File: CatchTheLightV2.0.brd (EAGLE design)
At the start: 45 x 100 mm, 42 parts, among them J1 TC2030-IDC-NL, U1 ATMEGA328PB-MUR

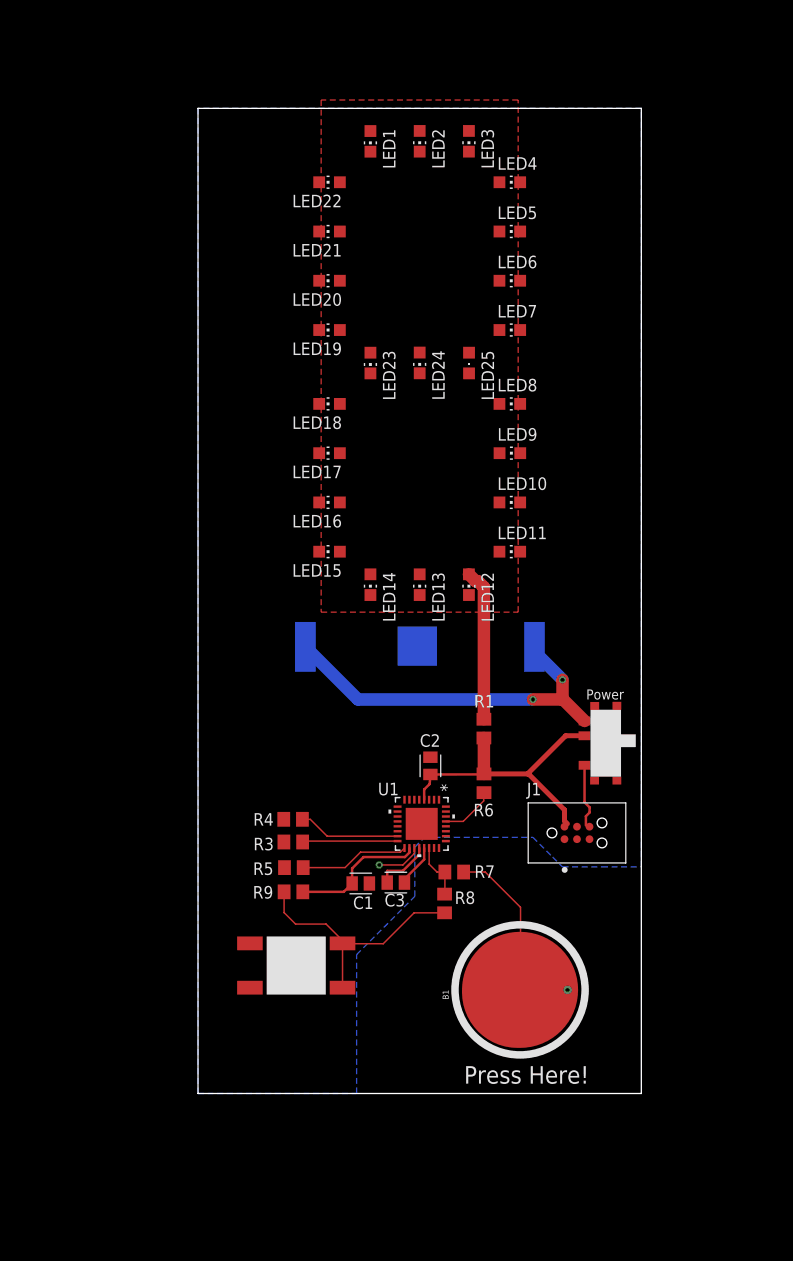
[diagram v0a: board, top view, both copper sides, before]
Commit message: Revised Schematic and Board design to use correct 328pb footprint
Modified a whole lot. New approach to board design. Will try to fill in all wiring first, and then draw in the rest of the pours/planes
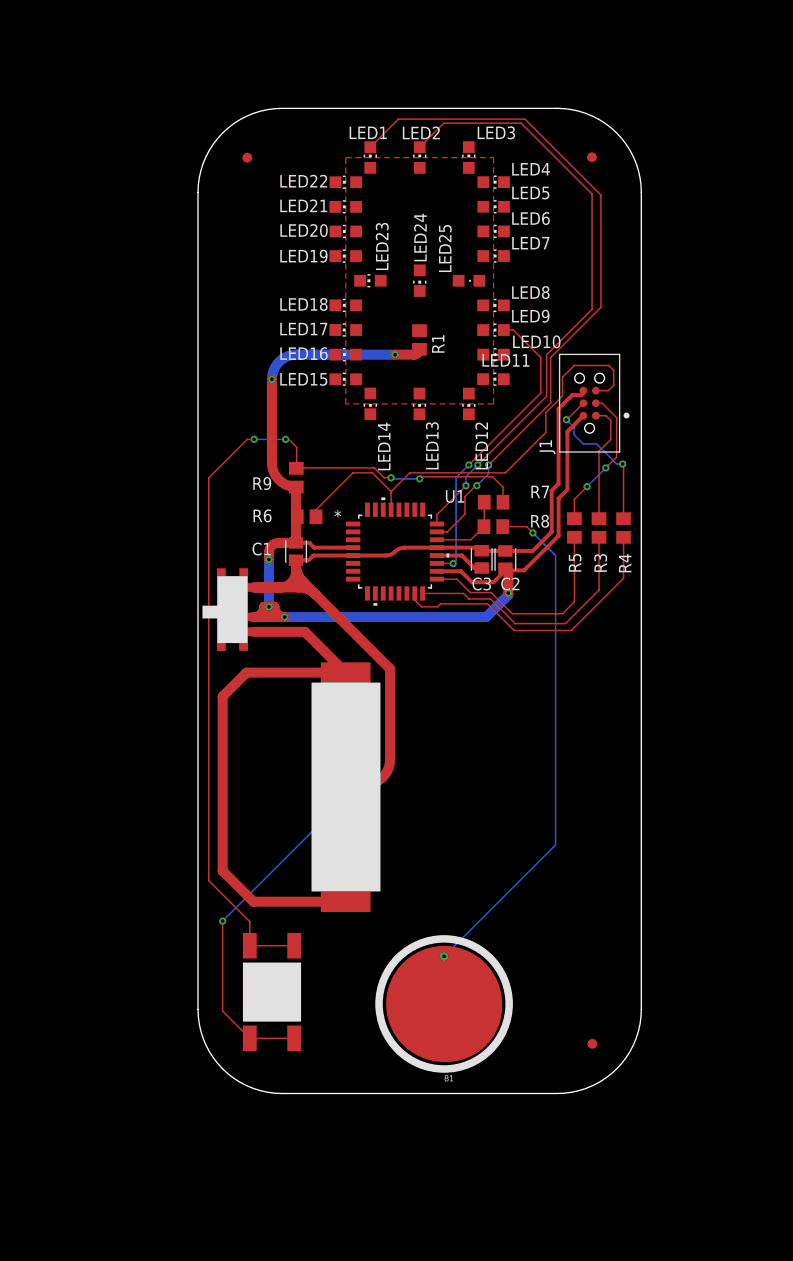
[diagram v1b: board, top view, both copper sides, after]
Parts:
- removed U$1: SK-3296S-01-L1, CustomParts:SK-3296S-01-L1
- removed U$2: TS-1102S-C-A-B, CustomParts:TS-1102S-C-A-B
- removed U$3: RK-2032, CustomParts:RK-2032
- added BAT1: RK-2032, ECE_388_CustomParts_V1.1:RK-2032
- added PB1: SK-3296S-01-L1, ECE_388_CustomParts_V1.1:SK-3296S-01-L1
- added PB2: PB2, ECE_388_CustomParts_V1.1:TS-1102S-C-A-B
- added U$4, U$5, U$6: FIDUCIAL, ECE388:FIDUCIAL_1MM
- U1: value ATMEGA328PB-MUR -> ATMEGA328PB-ANR; device 328PBMUR:32M1-A_MCH -> ECE_388_CustomParts_V1.1:32A_MCH
- moved R5 44.7 mm to (38.2, 57.4), turned to 90 degrees
- moved R4 44.7 mm to (43.2, 57.4), turned to 90 degrees
- moved R3 44.5 mm to (40.7, 57.4), turned to 90 degrees
- moved J1 43.6 mm to (39.8, 70.1), turned to 90 degrees
- moved R9 42.0 mm to (9.98, 62.5), turned to 270 degrees
- moved R8 41.0 mm to (30.0, 60.0), turned to 180 degrees
- moved R1 40.0 mm to (22.5, 76.5)
- moved R7 35.3 mm to (30.0, 57.5)
- moved C1 34.3 mm to (9.95, 55.0), turned to 270 degrees
- moved C3 33.9 mm to (28.8, 54.2), turned to 90 degrees
- moved R6 32.5 mm to (11.0, 58.5), turned to 180 degrees
- moved U1 27.8 mm to (20.0, 55.0), turned to 0 degrees
- moved C2 22.3 mm to (31.2, 54.2)
- moved LED14 18.4 mm to (17.5, 70.0)
- moved LED13 18.3 mm to (22.5, 70.0)
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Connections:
- removed net EPAD: U1.33
- net GND: now also BAT1.P$3, PB1.P1, PB2.3, PB2.4; no longer U$1.P1, U$2.3, U$2.4, U$3.P$3
- net SPARE_BUTTON_SIGNAL: now also PB2.1, PB2.2; no longer U$2.1, U$2.2
- net VCC_BATTERY: now also BAT1.P$1, BAT1.P$2, PB1.P3; no longer U$1.P3, U$3.P$1, U$3.P$2
- net VCC_TARGET: now also PB1.P2; no longer U$1.P2
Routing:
- net GND: track 10.8 -> 121.9 mm, vias 0 -> 2
- net PC0: track 0.00 -> 69.5 mm, vias 0 -> 2
- net VCC_TARGET: track 44.3 -> 110.6 mm, vias 0 -> 6
- net SPARE_BUTTON_SIGNAL: track 25.7 -> 90.2 mm, vias 0 -> 4
- net PC1: track 0.00 -> 61.5 mm, vias 0 -> 2
- net ~RESET/DW1: track 5.64 -> 46.4 mm
- net PE2: track 4.60 -> 31.1 mm, vias 1 -> 2
- net QTOUCH: track 26.3 -> 52.0 mm, vias 0 -> 1
- net PB3: track 10.4 -> 29.7 mm
- net VCC_BATTERY: track 38.0 -> 56.0 mm, vias 2 -> 0
- net PB4: track 9.67 -> 25.9 mm
- net MOSI: track 0.00 -> 16.0 mm, vias 0 -> 2
- net LED_ANODE: track 15.5 -> 0.00 mm
- net SCK: track 0.00 -> 14.7 mm, vias 0 -> 2
- net MISO: track 0.00 -> 12.1 mm
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- removed copper zone on layer 16, net GND
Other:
- outline, holes or cut-outs redrawn
- board text removed: "Power"
- board text removed: "Press Here!"

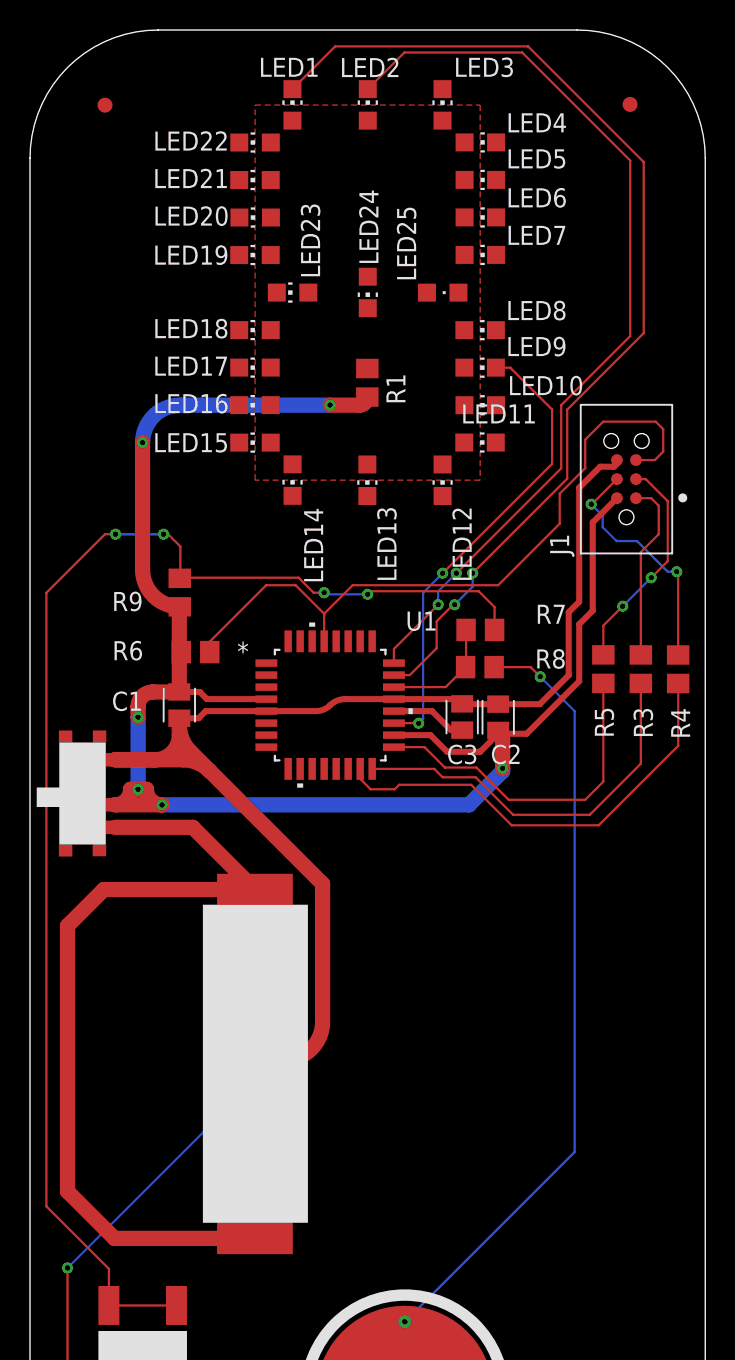
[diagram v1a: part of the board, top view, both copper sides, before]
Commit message: Finished Routing V1
Routing finished, no gnd planes yet
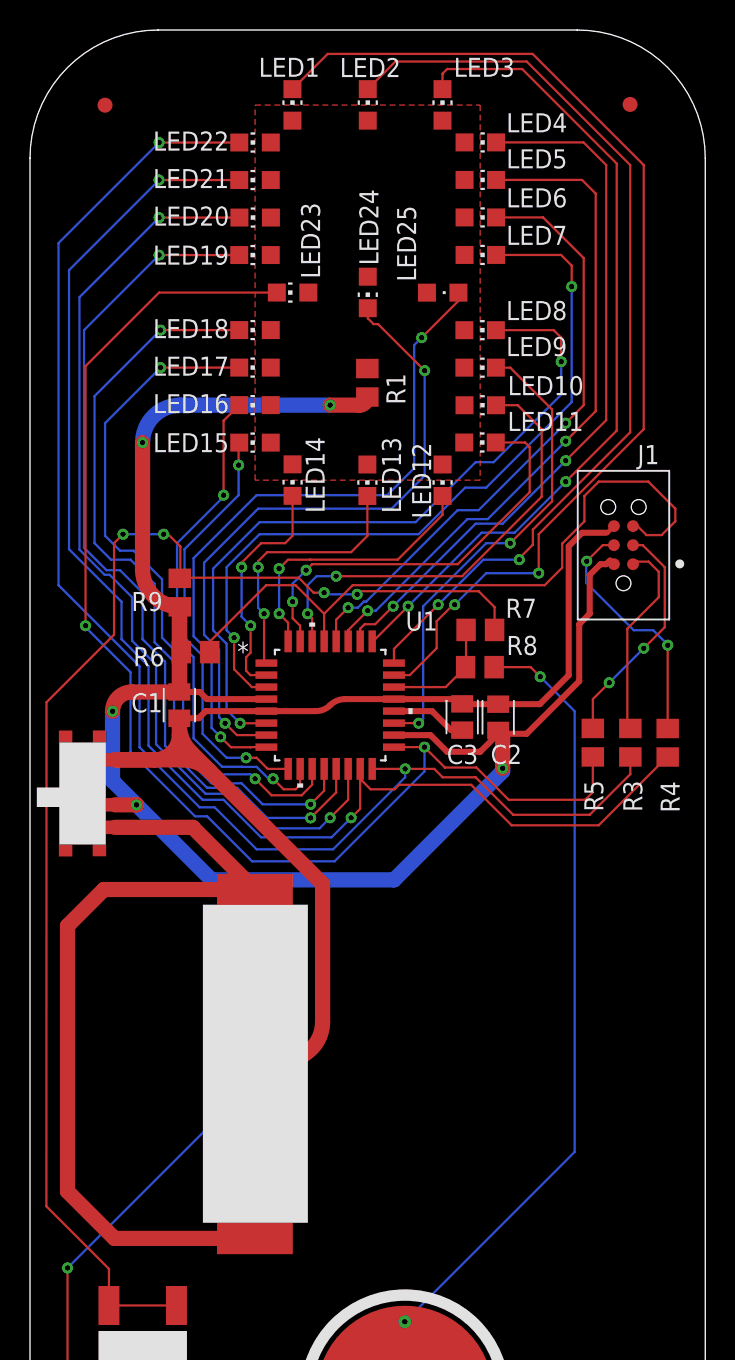
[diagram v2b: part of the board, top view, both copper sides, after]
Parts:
- moved R3 4.95 mm to (40.0, 52.5)
- moved R4 4.95 mm to (42.5, 52.5)
- moved R5 4.95 mm to (37.5, 52.5)
- moved J1 4.40 mm to (39.5, 65.7)
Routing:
- net PB4: track 25.9 -> 94.5 mm, vias 0 -> 2
- net PB5: track 22.5 -> 85.7 mm, vias 0 -> 2
- net PB2: track 0.00 -> 62.9 mm, vias 0 -> 2
- net PB3: track 29.7 -> 92.4 mm, vias 0 -> 2
- net PB1: track 0.00 -> 58.5 mm, vias 0 -> 2
- net PC2: track 0.00 -> 55.3 mm, vias 0 -> 2
- net PE0: track 0.00 -> 51.6 mm, vias 0 -> 2
- net PB0: track 0.00 -> 51.2 mm, vias 0 -> 2
- net PE1: track 0.00 -> 49.2 mm, vias 0 -> 2
- net PC3: track 0.00 -> 48.0 mm, vias 0 -> 2
- net PB7: track 0.00 -> 46.1 mm, vias 0 -> 2
- net PD7: track 0.00 -> 45.7 mm, vias 0 -> 2
- net PC4: track 0.00 -> 44.8 mm, vias 0 -> 2
- net PB6: track 0.00 -> 44.4 mm, vias 0 -> 2
- net PC5: track 0.00 -> 40.6 mm, vias 0 -> 2
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
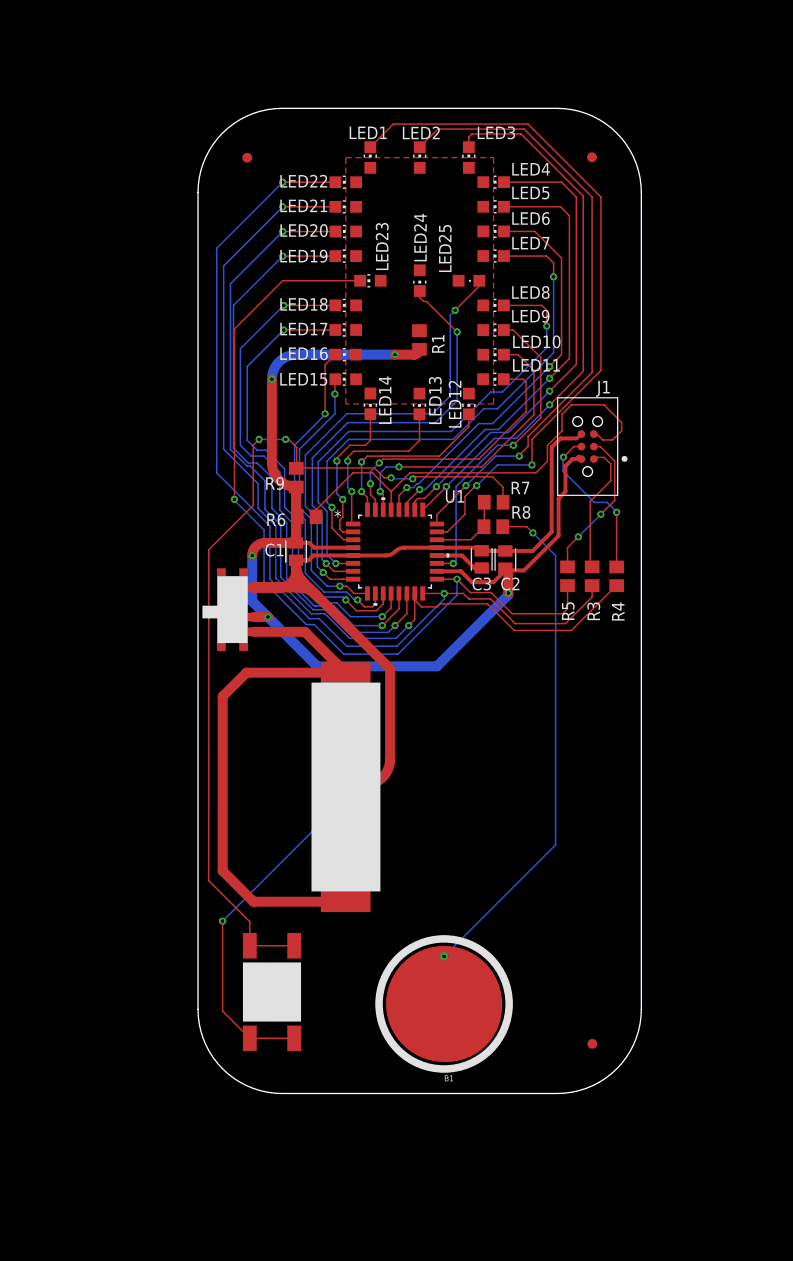
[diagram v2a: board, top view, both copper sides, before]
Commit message: Schematic pdf updated and put in renders
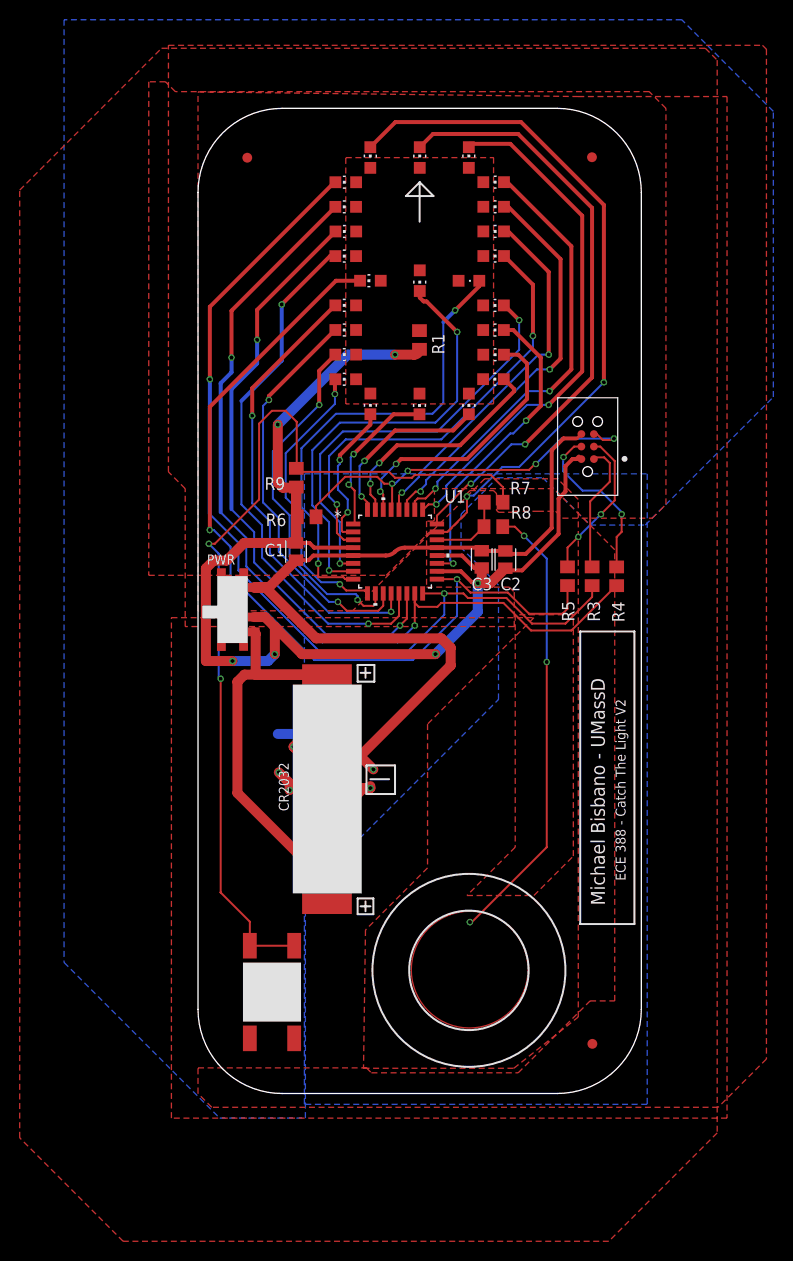
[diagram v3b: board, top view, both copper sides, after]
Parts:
- removed B1: (no value), PatternAgents-TouchWidgets:BUTTON_PASSIVE_12MM
- moved BAT1 1.91 mm to (16.6, 20.3)
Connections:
- removed net AREF_TARGET: C3.1, U1.20
- net QTOUCH: no longer B1.BUTTON
- net VCC_TARGET: now also C3.1, U1.20
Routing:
- net VCC_TARGET: track 116.0 -> 136.3 mm, vias 5 -> 6
- net GND: track 117.9 -> 129.3 mm, vias 2 -> 9
- net VCC_BATTERY: track 56.0 -> 47.3 mm
- net ~RESET/DW1: track 46.5 -> 39.8 mm, vias 0 -> 4
- net PE1: track 49.2 -> 43.0 mm
- net QTOUCH: track 52.0 -> 46.1 mm, vias 1 -> 3
- net PE0: track 51.6 -> 45.9 mm
- net SPARE_BUTTON_SIGNAL: track 89.5 -> 95.0 mm, vias 4 -> 2
- net AREF_TARGET: track 5.07 -> 0.00 mm
- net PB0: track 51.2 -> 46.2 mm
- net PD7: track 45.7 -> 40.8 mm
- net PD1: track 27.8 -> 23.7 mm
- net PC4: track 44.8 -> 40.9 mm
- net PB1: track 58.5 -> 55.0 mm
- net PC3: track 48.0 -> 44.6 mm
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- added copper zone on layer 1, net GND
- added copper zone on layer 16, net GND
- added copper zone on layer 1, net QTOUCH
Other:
- board text added: "CR2032"
- board text added: "ECE 388 - Catch The Light V2"
- board text added: "Michael Bisbano - UMassD"
- board text added: "PWR"

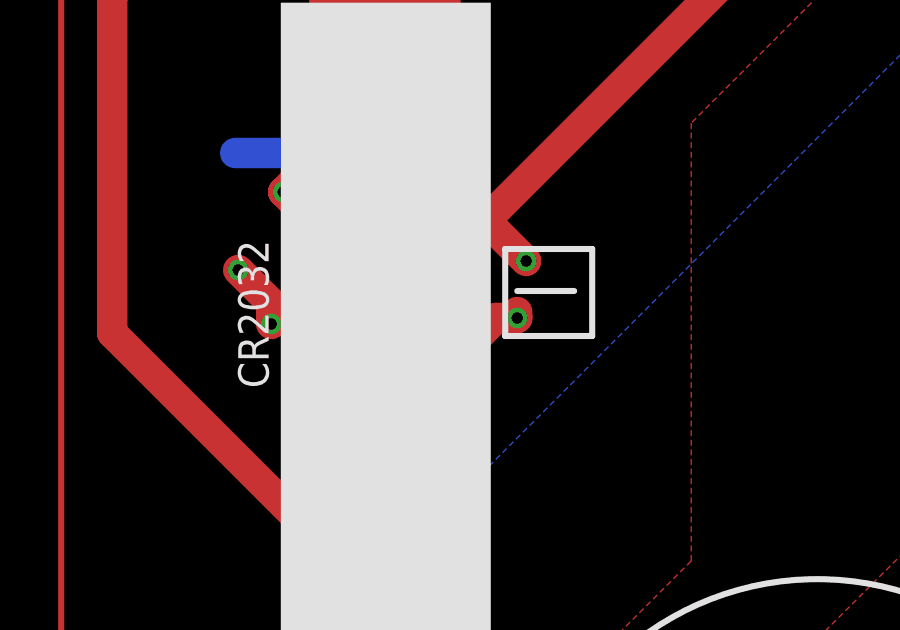
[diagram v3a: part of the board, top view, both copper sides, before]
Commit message: Board V1
First crack at board. Nervous about trace width for dissipating too much power. Also VERY unsure of qtouch button layout and traces.. We will see, will likely be modifying as the week goes on.
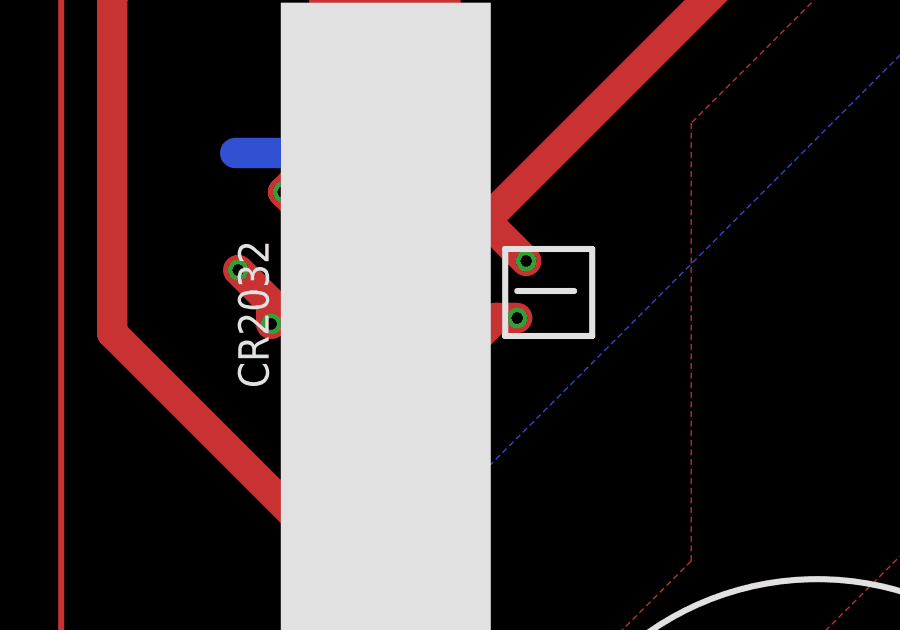
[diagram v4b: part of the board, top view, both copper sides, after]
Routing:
- net GND: track 129.3 -> 128.7 mm
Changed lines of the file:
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@@
 <wire x1="25.65" y1="45.25" x2="25.65" y2="43.45" width="1.016" layer="1"/>
 <wire x1="25.65" y1="43.45" x2="15.3" y2="33.1" width="1.016" layer="1"/>
-<wire x1="13.02" y1="31.16" x2="13.36" y2="31.16" width="1.016" layer="1"/>
 <polygon width="0.2032" layer="16" spacing="1.778" pour="hatch" thermals="no" rank="2">
 <vertex x="10.8" y="-1.1"/>
@@
 <wire x1="17.8" y1="32.9" x2="15.8" y2="34.9" width="1.016" layer="1"/>
 <wire x1="15.8" y1="34.9" x2="15.8" y2="35.8" width="1.016" layer="1"/>
-<wire x1="17.5" y1="31.2" x2="17.5" y2="31" width="1.016" layer="1"/>
 <polygon width="0.2032" layer="1" spacing="0.254" rank="3">
 <vertex x="-2.7" y="48.3"/>

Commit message: Schematic Submission Issues addressed
Changes documented in issue
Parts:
- added SJ1: (no value), ECE388:SJW
- added U$1: SCHOTTKY_SS14L, ECE_388_CustomParts_V1.1:SOD123FL
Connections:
- net VCC_TARGET renamed VCC
- new net PROTECTED_VBAT: PB1.P3, SJ1.2, U$1.C
- net VCC_BATTERY: now also SJ1.1, U$1.A; no longer PB1.P3
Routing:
- net GND: track 128.7 -> 44.7 mm, vias 9 -> 16
- net PROTECTED_VBAT: track 0.00 -> 27.5 mm
- net VCC_BATTERY: track 47.3 -> 38.3 mm
- net VCC: track 136.3 -> 130.2 mm
- net MISO: track 13.4 -> 12.8 mm
